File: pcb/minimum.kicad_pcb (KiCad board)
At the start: 4 copper layers, 16 x 22 mm, 36 parts, among them J1 DX07P024MJ1R1500, SW1 SW_Push, U1 RP2040, U2 SCD4x, U3 W25Q16JVUXIQ, U4 XCL220, Y1 C2E-12.000-18-1020-X-R

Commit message: DRC OK
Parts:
- moved R2 0.99 mm to (98.3, 66.0)
- moved R1 0.99 mm to (99.3, 66.0)
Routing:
- net /USB_D-: track 0.00 -> 9.94 mm, vias 0 -> 1
- net /USB_D+: track 0.00 -> 9.90 mm, vias 0 -> 1
- net +1V1: track 20.4 -> 17.0 mm
- net GND: track 21.9 -> 25.0 mm, vias 9 -> 10
- net /Pi_USB_D+: track 0.00 -> 1.44 mm
- net /Pi_USB_D-: track 0.00 -> 1.44 mm
- net VBUS: track 10.9 -> 10.3 mm
- net +3V3: track 51.0 -> 51.5 mm
- added copper zone on In1.Cu, net GND

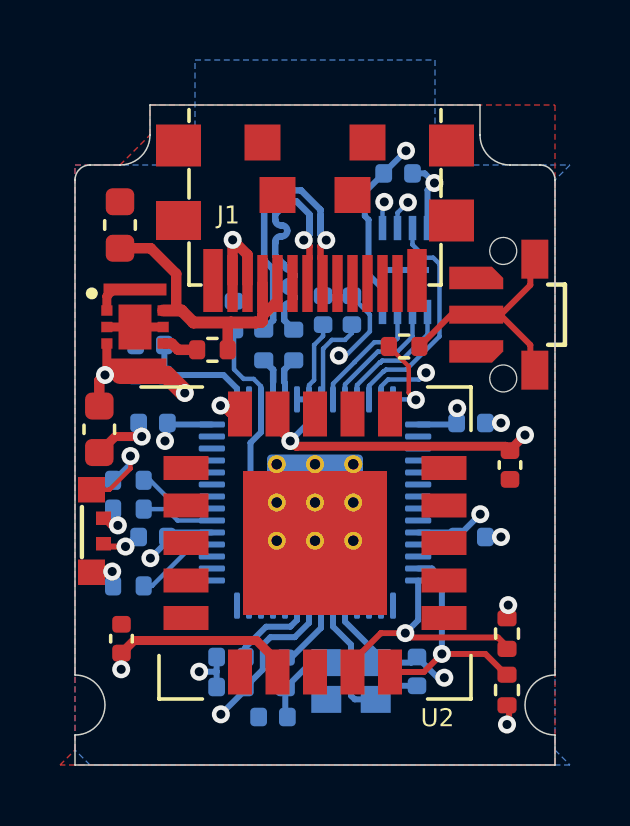
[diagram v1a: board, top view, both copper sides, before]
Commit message: CanAir.IO logo added
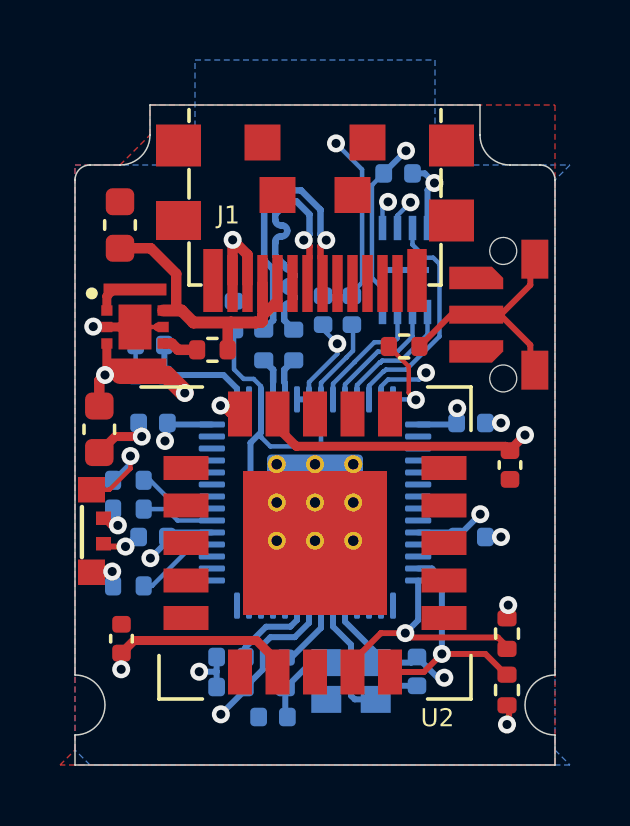
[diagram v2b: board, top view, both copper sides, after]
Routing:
- net GND: track 25.0 -> 30.5 mm, vias 10 -> 11
- net +1V1: track 17.0 -> 20.9 mm
- net +3V3: track 51.5 -> 49.9 mm
- net /USB_D-: track 9.94 -> 8.44 mm
- net /USB_D+: track 9.90 -> 8.40 mm

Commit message: OpenHardware logo added
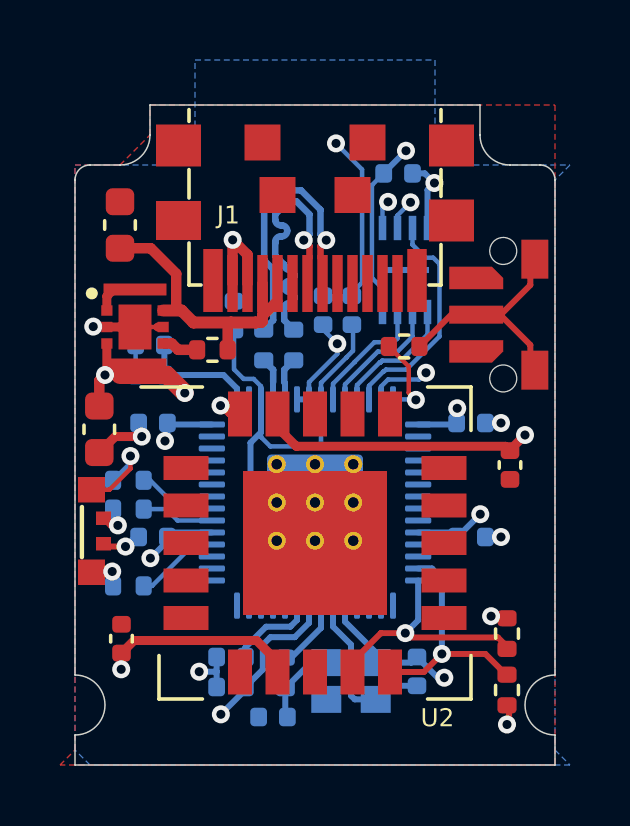
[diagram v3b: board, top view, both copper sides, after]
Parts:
- added LOGO1: LOGO, SMD:CanAir_IO, B.Cu at (97.6, 60.9)
- added LOGO2: Logo_Open_Hardware_Small, SMD:OHW_LOGO, B.Cu at (105.9, 74.9)

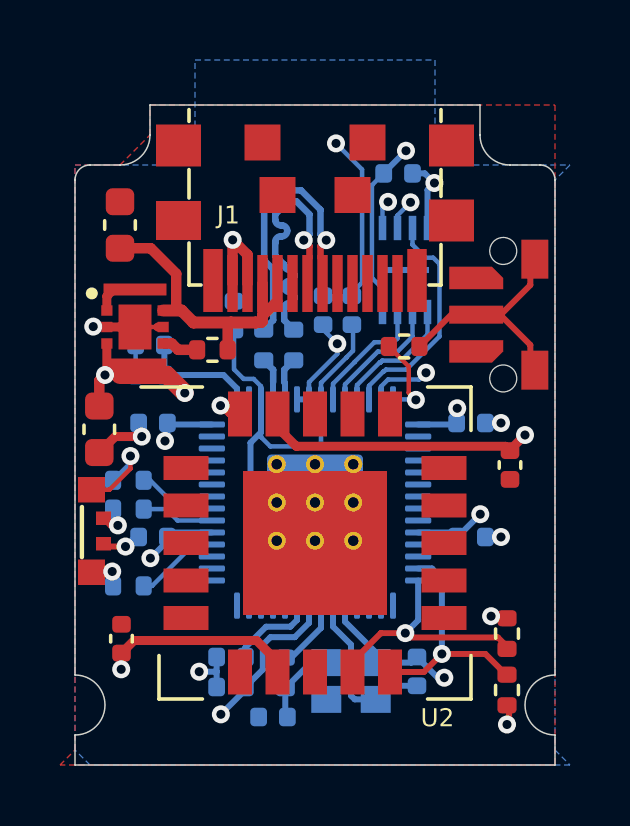
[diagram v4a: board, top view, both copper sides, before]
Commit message: Fix common pin RGB Led
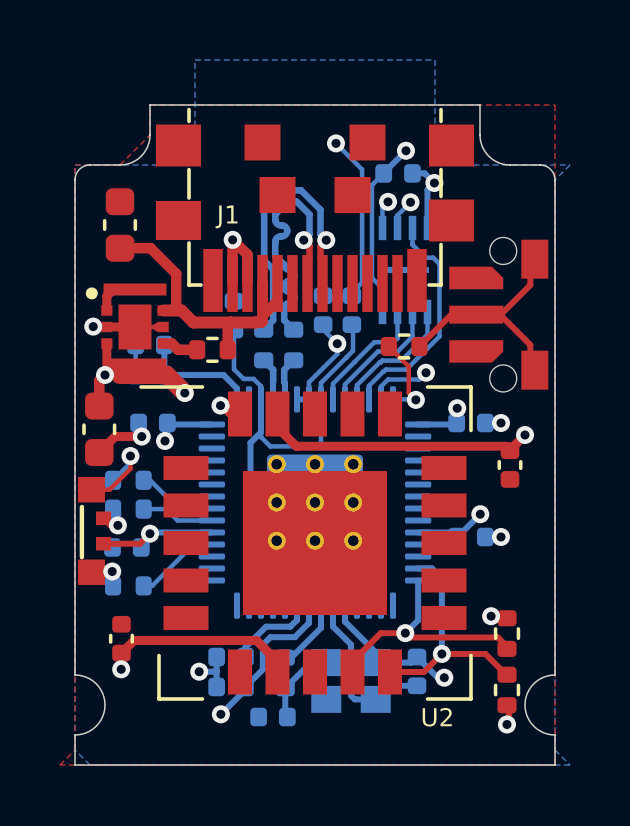
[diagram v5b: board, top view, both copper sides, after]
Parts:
- moved C2 0.94 mm to (93.7, 72.8)
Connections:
- D1 pad 2: GND -> +3V3
- J1 pad A10: (no net) -> unconnected-(J1-PadA10)
- J1 pad A11: (no net) -> unconnected-(J1-PadA11)
- J1 pad A5: (no net) -> unconnected-(J1-PadA5)
- J1 pad B2: (no net) -> unconnected-(J1-PadB2)
- J1 pad B3: (no net) -> unconnected-(J1-PadB3)
- J1 pad B5: (no net) -> unconnected-(J1-PadB5)
- U1 pad 11: (no net) -> unconnected-(U1-Pad11)
- U1 pad 12: (no net) -> unconnected-(U1-Pad12)
- U1 pad 15: (no net) -> unconnected-(U1-Pad15)
- U1 pad 16: (no net) -> unconnected-(U1-Pad16)
- U1 pad 17: (no net) -> unconnected-(U1-Pad17)
- U1 pad 18: (no net) -> unconnected-(U1-Pad18)
- U1 pad 2: (no net) -> unconnected-(U1-Pad2)
- U1 pad 24: (no net) -> unconnected-(U1-Pad24)
- U1 pad 25: (no net) -> unconnected-(U1-Pad25)
- U1 pad 26: (no net) -> /RUN
- U1 pad 27: (no net) -> unconnected-(U1-Pad27)
- U1 pad 28: (no net) -> unconnected-(U1-Pad28)
- U1 pad 29: (no net) -> unconnected-(U1-Pad29)
- U1 pad 3: (no net) -> unconnected-(U1-Pad3)
- U1 pad 30: (no net) -> unconnected-(U1-Pad30)
- U1 pad 31: (no net) -> unconnected-(U1-Pad31)
- U1 pad 36: (no net) -> unconnected-(U1-Pad36)
- U1 pad 37: (no net) -> unconnected-(U1-Pad37)
- U1 pad 38: (no net) -> unconnected-(U1-Pad38)
- U1 pad 39: (no net) -> unconnected-(U1-Pad39)
- U1 pad 4: (no net) -> unconnected-(U1-Pad4)
- U1 pad 40: (no net) -> unconnected-(U1-Pad40)
- U1 pad 41: (no net) -> unconnected-(U1-Pad41)
- U1 pad 5: (no net) -> unconnected-(U1-Pad5)
- U1 pad 6: (no net) -> unconnected-(U1-Pad6)
- U1 pad 7: (no net) -> unconnected-(U1-Pad7)
- U1 pad 8: (no net) -> unconnected-(U1-Pad8)
- U1 pad 9: (no net) -> unconnected-(U1-Pad9)
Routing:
- net +3V3: track 50.0 -> 52.2 mm
- net GND: track 30.5 -> 29.4 mm, vias 11 -> 10
